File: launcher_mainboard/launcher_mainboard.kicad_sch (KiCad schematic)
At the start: 79 parts, among them J1 USB_B_Micro, J10 pin headers, J2 Conn_01x06, J3 Conn_01x06, J4 Conn_01x06, J5 Conn_01x06, J6 bat_con, J7 fan_con, J8 ESC_1, J9 ESC_2, Q1 2N7002H, Q2 2N3904, Q3 2N3904, Q4 BSS138, Q5 BSS138, Q6 BSS138, Q7 BSS138, SW1 POWER_SWITCH, U1 ESP32-S3-MINI-1, U12 LM66200DRLR, U2 TMC2209-LA-T, U3 TMC2209-LA-T, U4 TMC2209-LA-T, U5 TMC2209-LA-T, U6 TLV75801PDRV, U7 R-78E3.3-0.5, U8 D3V3XA4B10LP, U9 R-78E5.0-0.5

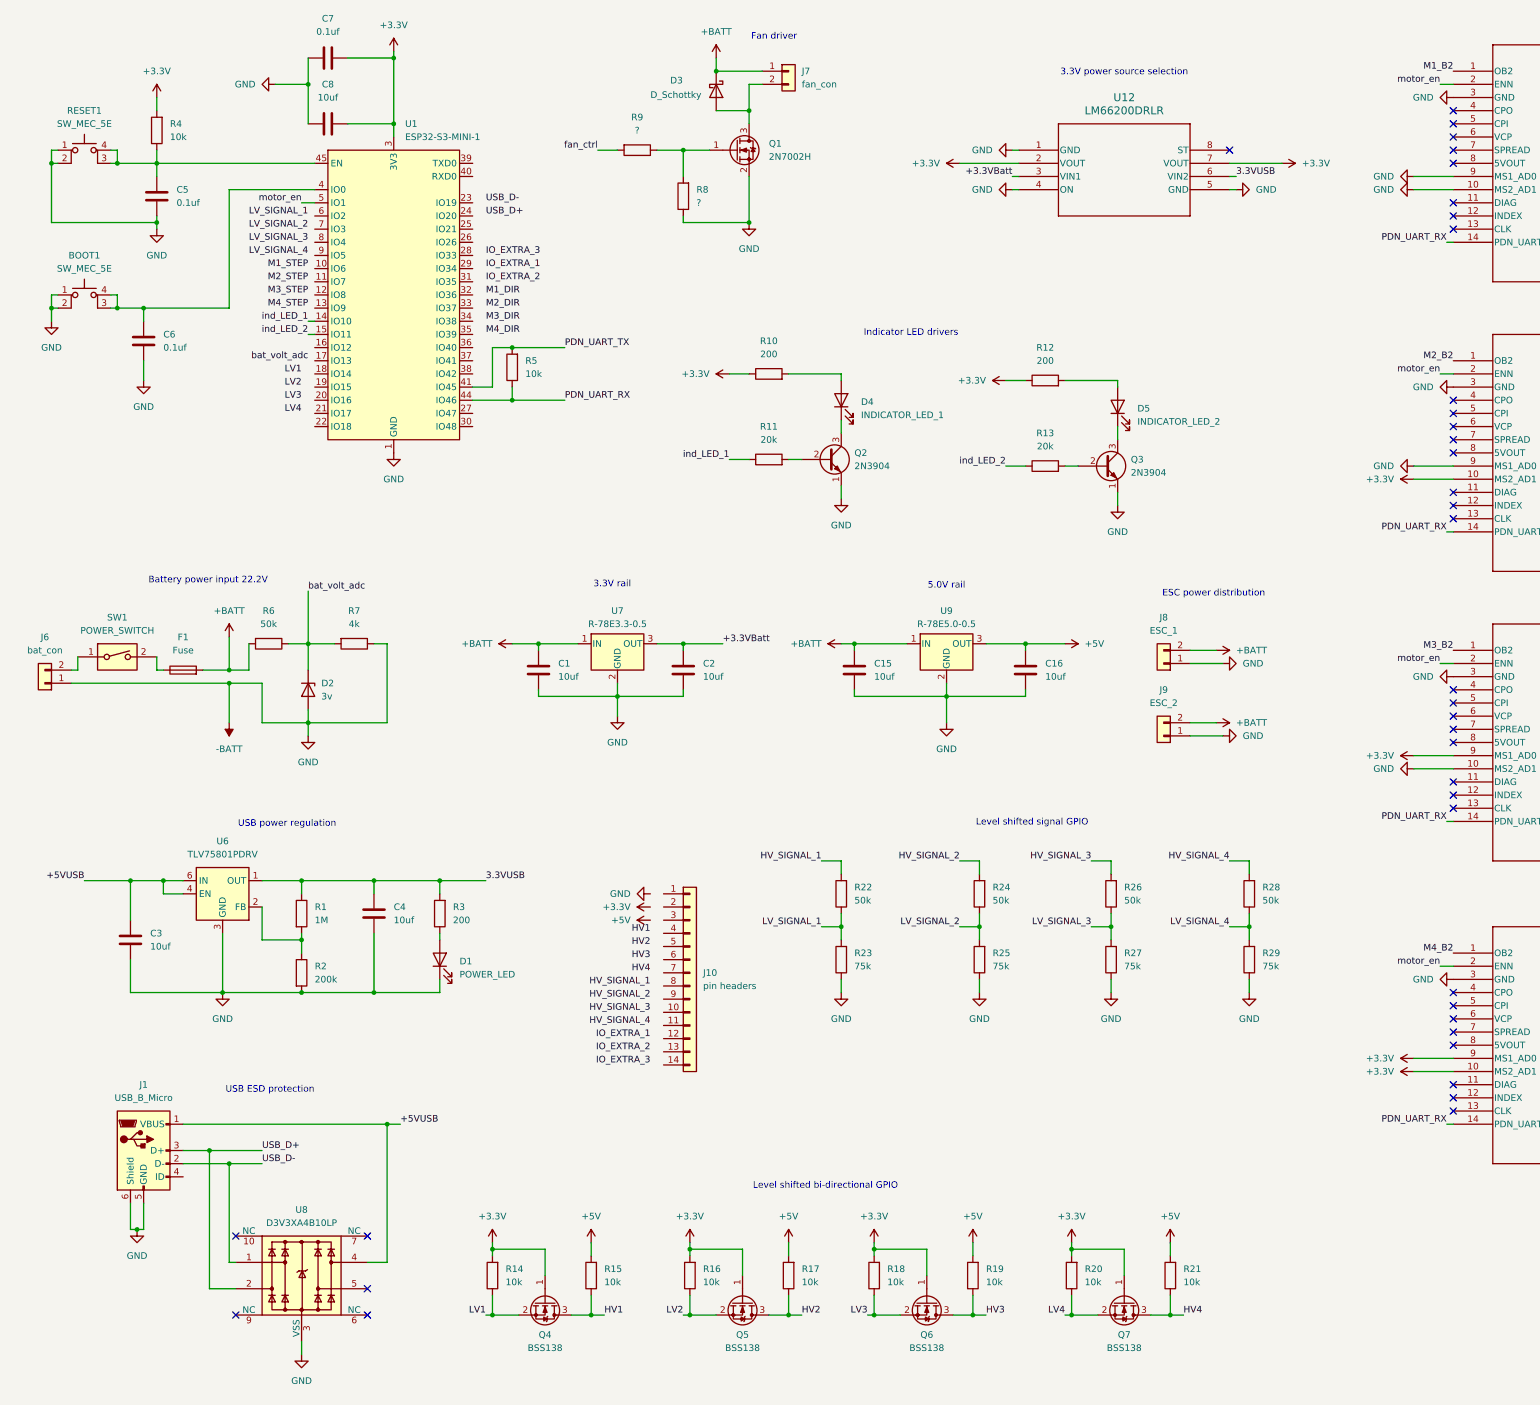
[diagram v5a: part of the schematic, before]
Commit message: first complete scematic draft
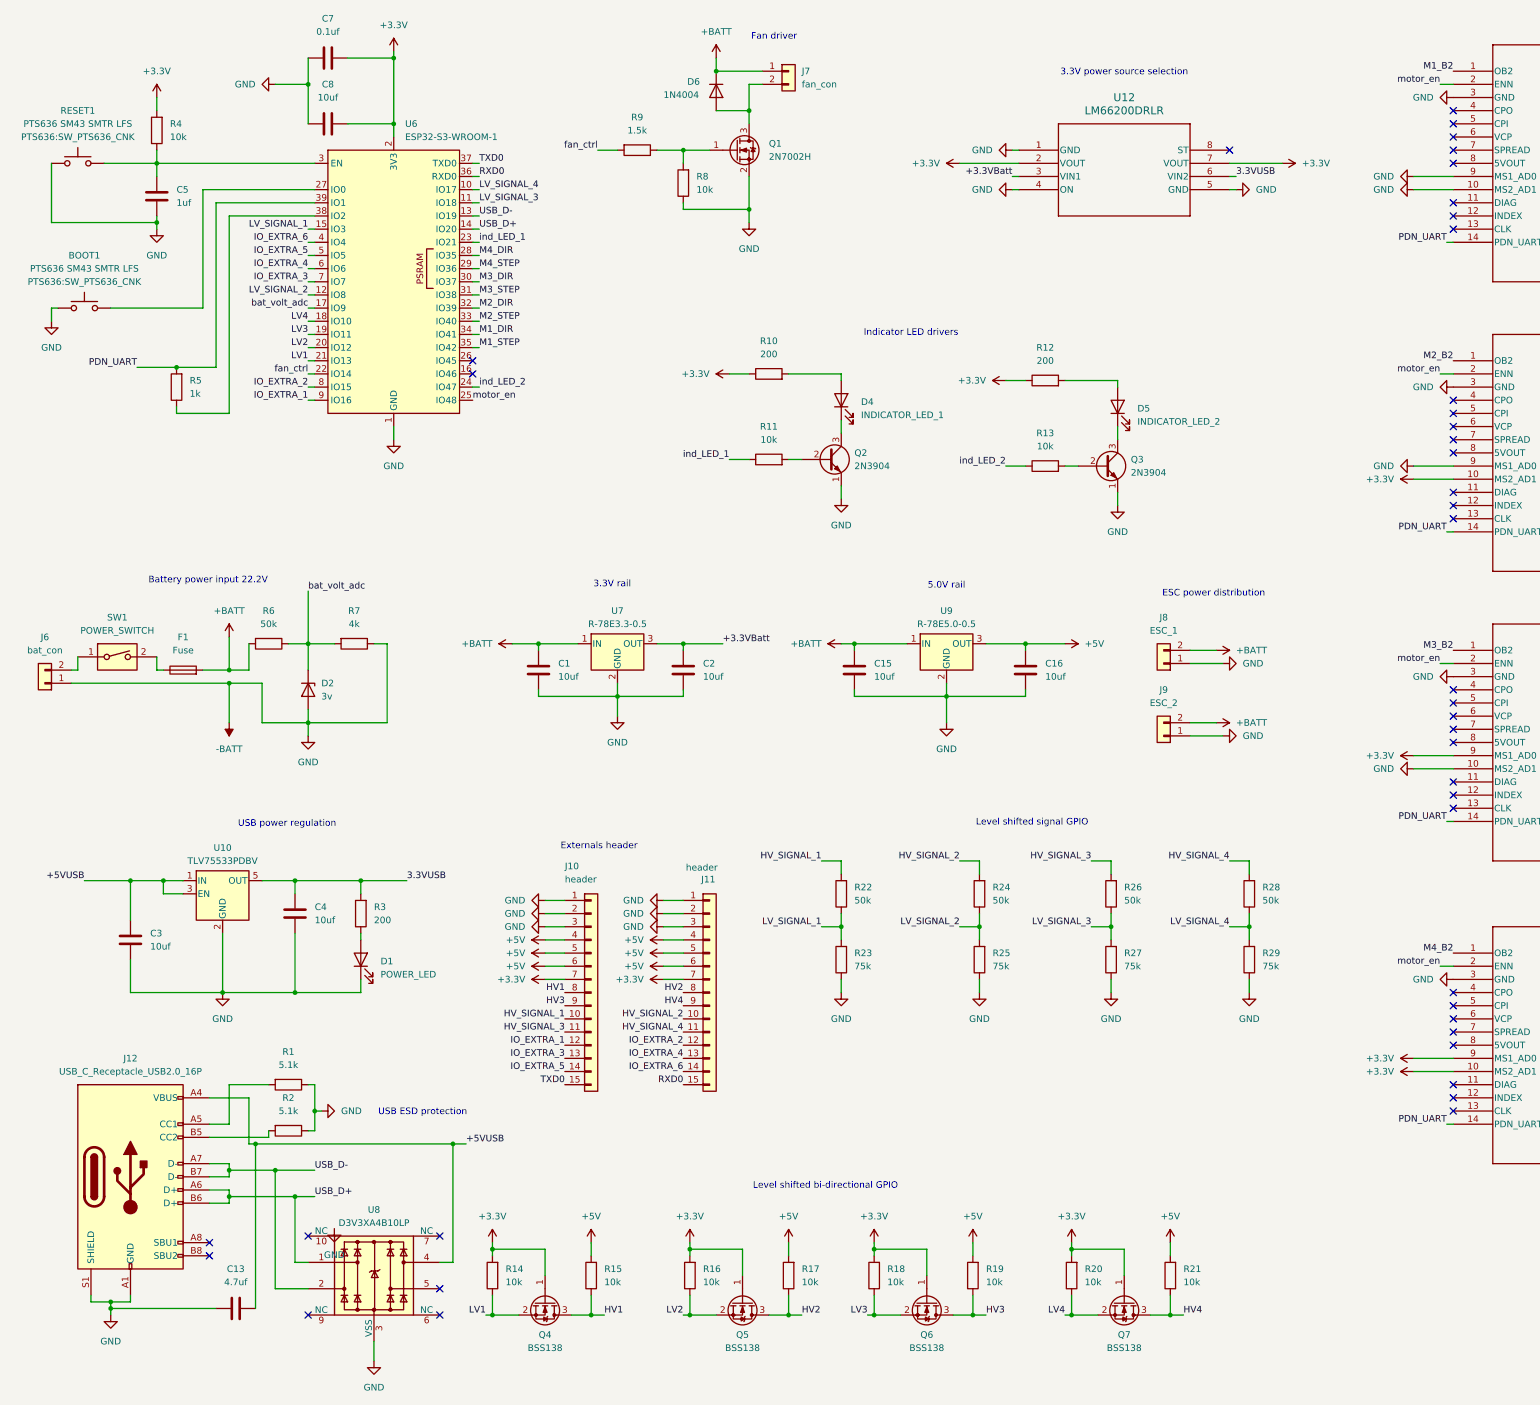
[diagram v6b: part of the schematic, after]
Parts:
- removed BOOT1, RESET1: SW_MEC_5E, Button_Switch_SMD:SW_MEC_5GSH9, symbol Switch:SW_MEC_5E
- removed C6: 0.1uf, Capacitor_SMD:C_0201_0603Metric, symbol Device:C
- removed D3: D_Schottky, Diode_SMD:D_0201_0603Metric, symbol Device:D_Schottky
- removed J1: USB_B_Micro, Connector_USB:USB_Micro-B_Amphenol_10104110_Horizontal, symbol Connector:USB_B_Micro
- removed J10: pin headers, Connector_PinHeader_2.54mm:PinHeader_1x14_P2.54mm_Vertical, symbol Connector_Generic:Conn_01x14
- removed U1: ESP32-S3-MINI-1, RF_Module:ESP32-S2-MINI-1, symbol RF_Module:ESP32-S3-MINI-1
- removed U6: TLV75801PDRV, Package_SON:WSON-6-1EP_2x2mm_P0.65mm_EP1x1.6mm, symbol Regulator_Linear:TLV75801PDRV
- added BOOT1, RESET1: PTS636 SM43 SMTR LFS, PTS636:SW_PTS636_CNK, symbol Switch:SW_Push
- added C13: 4.7uf, Capacitor_SMD:C_0805_2012Metric, symbol Device:C
- added D6: 1N4004, Diode_THT:D_DO-35_SOD27_P5.08mm_Vertical_KathodeUp, symbol Diode:1N4004
- added J10, J11: header, Connector_PinHeader_2.54mm:PinHeader_1x15_P2.54mm_Vertical, symbol Connector_Generic:Conn_01x15
- added J12: USB_C_Receptacle_USB2.0_16P, Connector_USB:USB_C_Receptacle_G-Switch_GT-USB-7010ASV, symbol Connector:USB_C_Receptacle_USB2.0_16P
- added U10: TLV75533PDBV, Package_TO_SOT_SMD:SOT-23-5, symbol Regulator_Linear:TLV75533PDBV
- added U6: ESP32-S3-WROOM-1, RF_Module:ESP32-S3-WROOM-1, symbol RF_Module:ESP32-S3-WROOM-1
- C1, C15, C16, C2, C3, C4, C7, C8: footprint Capacitor_SMD:C_0201_0603Metric -> Capacitor_SMD:C_0805_2012Metric
- C5: value 0.1uf -> 1uf; footprint Capacitor_SMD:C_0201_0603Metric -> Capacitor_SMD:C_0805_2012Metric
- R1: value 1M -> 5.1k; footprint Resistor_SMD:R_0201_0603Metric -> Resistor_SMD:R_0805_2012Metric
- R10, R12, R14, R15, R16, R17, R18, R19, R20, R21, R22, R23, R24, R25, R26, R27, R28, R29, R3, R4, R6, R7: footprint Resistor_SMD:R_0201_0603Metric -> Resistor_SMD:R_0805_2012Metric
- R11, R13: value 20k -> 10k; footprint Resistor_SMD:R_0201_0603Metric -> Resistor_SMD:R_0805_2012Metric
- R2: value 200k -> 5.1k; footprint Resistor_SMD:R_0201_0603Metric -> Resistor_SMD:R_0805_2012Metric
- R5: value 10k -> 1k; footprint Resistor_SMD:R_0201_0603Metric -> Resistor_SMD:R_0805_2012Metric
- R8: value ? -> 10k; footprint Resistor_SMD:R_0201_0603Metric -> Resistor_SMD:R_0805_2012Metric
- R9: value ? -> 1.5k; footprint Resistor_SMD:R_0201_0603Metric -> Resistor_SMD:R_0805_2012Metric
- SW1: footprint (none) -> Button_Switch_SMD:SW_DIP_SPSTx01_Slide_9.78x4.72mm_W8.61mm_P2.54mm
- U3, U4, U5: footprint TMC2209-LA-T:QFN28_5X5_3X8_EPAD_TRI -> CustomFootprints:TCM2209_Module
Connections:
- net PDN_UART_TX is gone; now on net PDN_UART: R5.2
- net +3.3V: now also J10.7 (Pin_7), J11.7 (Pin_7), U6.2 (3V3)
- net +5V: now also J10.4 (Pin_4), J10.5 (Pin_5), J10.6 (Pin_6), J11.4 (Pin_4), J11.5 (Pin_5), J11.6 (Pin_6)
- net +5VUSB: now also C13.1, J12.A4 (VBUS), J12.A9 (VBUS), J12.B4 (VBUS), J12.B9 (VBUS), U10.1 (IN), U10.3 (EN)
- net +BATT: now also D6.1 (K)
- net -BATT: now also R1.1, R2.1, BOOT1.1, C13.2, J10.1 (Pin_1), J10.2 (Pin_2), J10.3 (Pin_3), J11.1 (Pin_1), J11.2 (Pin_2), J11.3 (Pin_3), J12.A1 (GND), J12.A12 (GND), J12.B1 (GND), J12.B12 (GND), J12.S1 (SHIELD), RESET1.1, U10.2 (GND), U6.1 (GND), U6.40 (GND), U6.41 (GND); no longer R2.2
- net 3.3VUSB: now also U10.5 (OUT); no longer R1.1
- net HV1: now also J10.8 (Pin_8)
- net HV2: now also J11.8 (Pin_8)
- net HV3: now also J10.9 (Pin_9)
- net HV4: now also J11.9 (Pin_9)
- net HV_SIGNAL_1: now also J10.10 (Pin_10)
- net HV_SIGNAL_2: now also J11.10 (Pin_10)
- net HV_SIGNAL_3: now also J10.11 (Pin_11)
- net HV_SIGNAL_4: now also J11.11 (Pin_11)
- net IO_EXTRA_1: now also J10.12 (Pin_12), U6.9 (IO16)
- net IO_EXTRA_2: now also J11.12 (Pin_12), U6.8 (IO15)
- net IO_EXTRA_3: now also J10.13 (Pin_13), U6.7 (IO7)
- net LV1: now also U6.21 (IO13)
- net LV2: now also U6.20 (IO12)
- net LV3: now also U6.19 (IO11)
- net LV4: now also U6.18 (IO10)
- net LV_SIGNAL_1: now also U6.15 (IO3)
- net LV_SIGNAL_2: now also U6.12 (IO8)
- net LV_SIGNAL_3: now also U6.11 (IO18)
- net LV_SIGNAL_4: now also U6.10 (IO17)
- net M1_DIR: now also U6.34 (IO41)
- net M1_STEP: now also U6.35 (IO42)
- net M2_DIR: now also U6.32 (IO39)
- net M2_STEP: now also U6.33 (IO40)
- net M3_DIR: now also U6.30 (IO37)
- net M3_STEP: now also U6.31 (IO38)
- net M4_DIR: now also U6.28 (IO35)
- net M4_STEP: now also U6.29 (IO36)
- net USB_D+: now also U8.1, J12.A6 (D+), J12.B6 (D+), U6.14 (IO20); no longer U8.2
- net USB_D-: now also U8.2, J12.A7 (D-), J12.B7 (D-), U6.13 (IO19); no longer U8.1
- net bat_volt_adc: now also U6.17 (IO9)
- net fan_ctrl: now also U6.22 (IO14)
- net ind_LED_1: now also U6.23 (IO21)
- net ind_LED_2: now also U6.24 (IO47)
- net motor_en: now also U6.25 (IO48)
- net at R1.2: now also J12.A5 (CC1); no longer R2.1
- net at J7.2 (Pin_2), Q1.3 (D): now also D6.2 (A)
- net at C5.1, R4.1: now also RESET1.2, U6.3 (EN)
- net PDN_UART_RX renamed PDN_UART
- net PDN_UART: now also U6.39 (IO1); no longer R5.1
- new net: J12.B5 (CC2), R2.2
- new net: BOOT1.2, U6.27 (IO0)
- new net: R5.1, U6.38 (IO2)
- new net IO_EXTRA_4: J11.13 (Pin_13), U6.6 (IO6)
- new net IO_EXTRA_5: J10.14 (Pin_14), U6.5 (IO5)
- new net IO_EXTRA_6: J11.14 (Pin_14), U6.4 (IO4)
- new net RXD0: J11.15 (Pin_15), U6.36 (RXD0)
- new net TXD0: J10.15 (Pin_15), U6.37 (TXD0)
- no-connect marks 54 -> 58
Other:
- note added: "Externals header"
- moved on the sheet: C4, D1, R3, R5, R8, U8

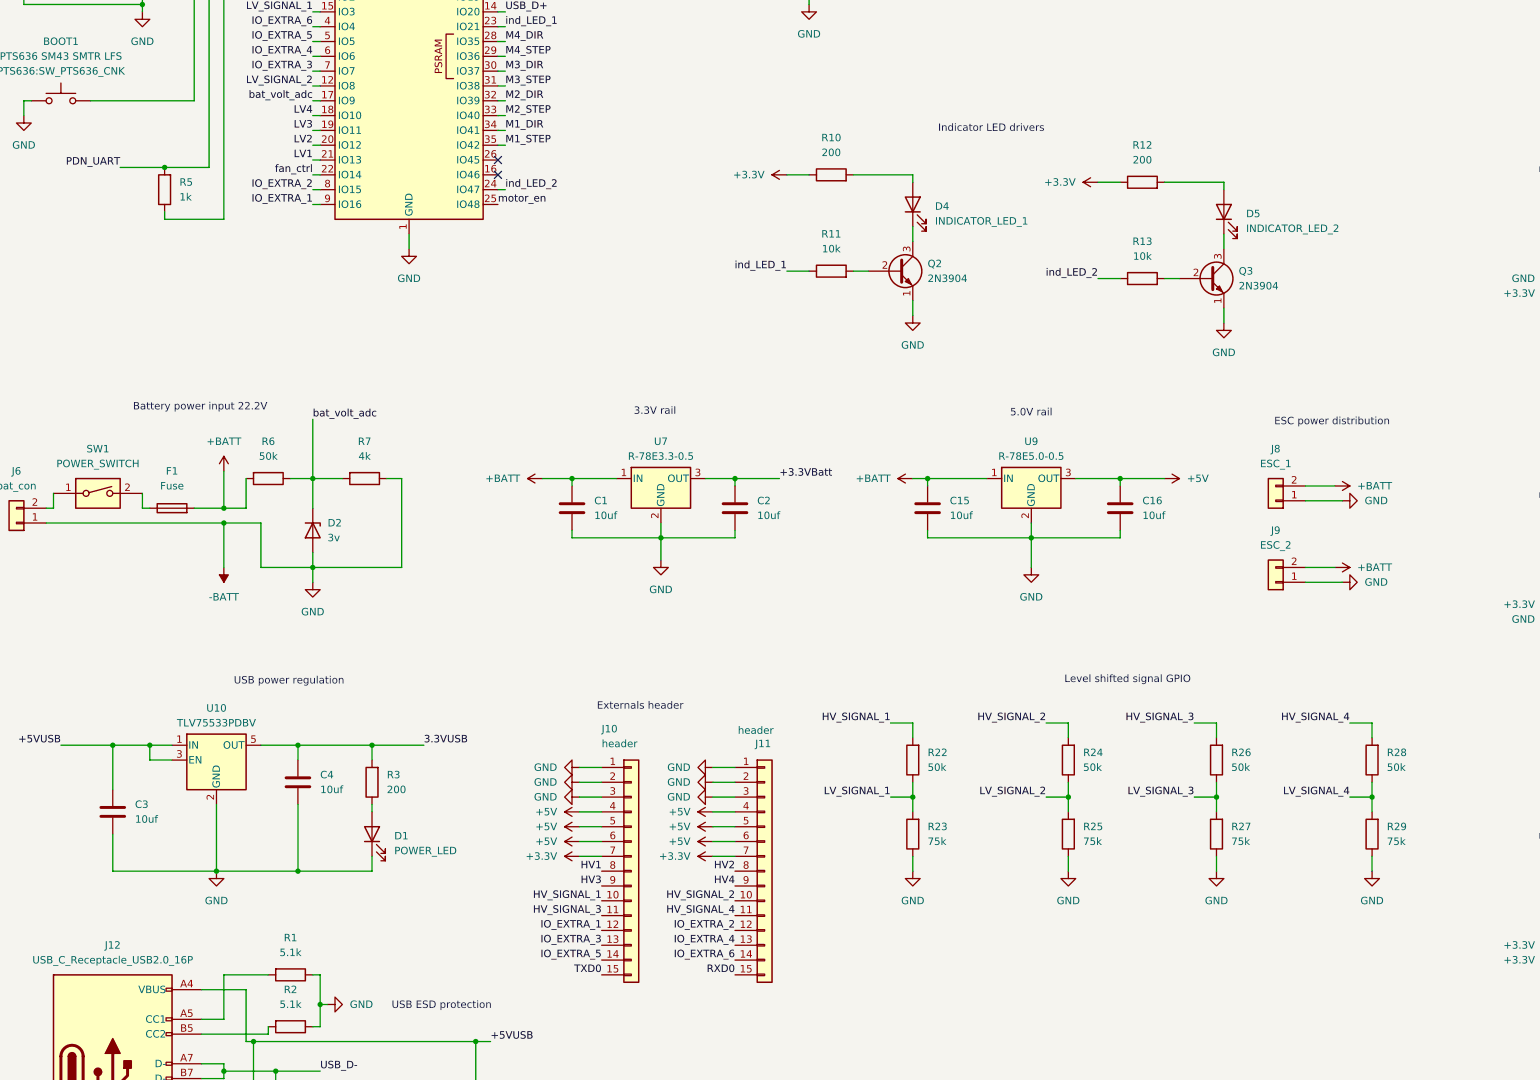
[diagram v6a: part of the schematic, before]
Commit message: added more footprints. Rought layout
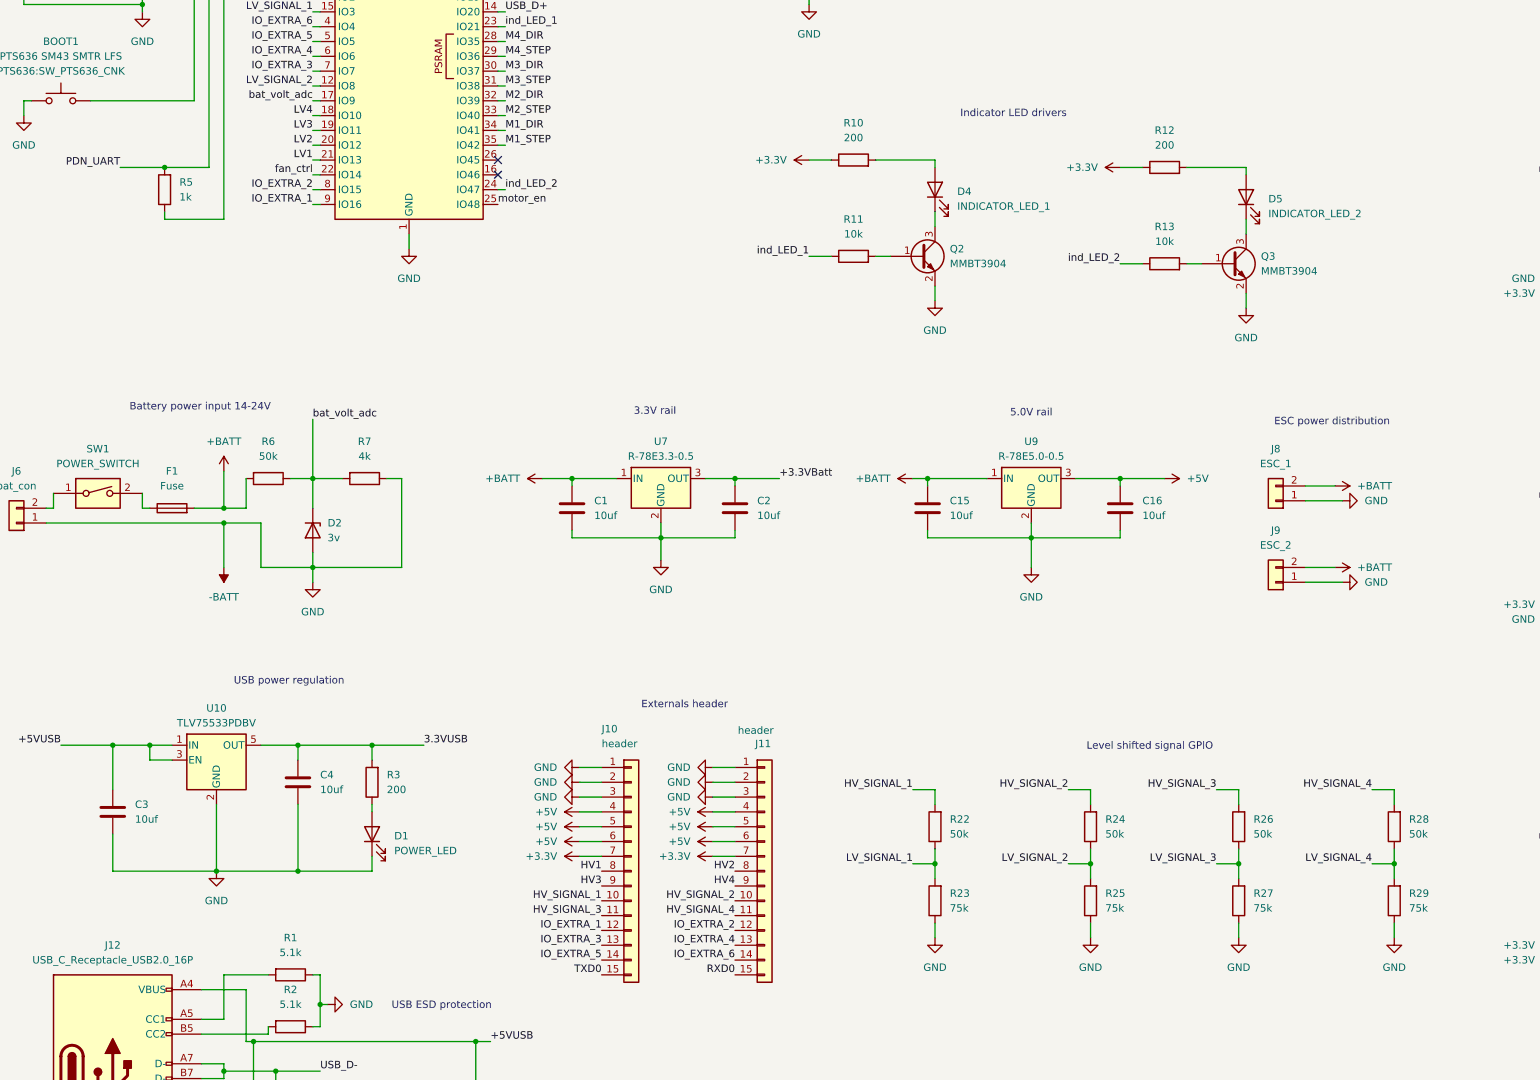
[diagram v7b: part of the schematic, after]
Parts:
- removed Q2, Q3: 2N3904, Package_TO_SOT_THT:TO-92_Inline, symbol Transistor_BJT:2N3904
- added Q2, Q3: MMBT3904, Package_TO_SOT_SMD:SOT-23, symbol Transistor_BJT:MMBT3904
- F1: footprint Fuse:FuseHolder_Blade_ATO_Littelfuse_FLR_178.6165 -> Fuse:Fuseholder_Clip-5x20mm_Bel_FC-203-22_Lateral_P17.80x5.00mm_D1.17mm_Horizontal
- J12: footprint Connector_USB:USB_C_Receptacle_G-Switch_GT-USB-7010ASV -> Connector_USB:USB_C_Receptacle_JAE_DX07S016JA1R1500
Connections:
- net -BATT: now also Q2.2 (E), Q3.2 (E)
- net at D4.1 (K): now also Q2.3 (C)
- net at R13.2: now also Q3.1 (B)
- net at D5.1 (K): now also Q3.3 (C)
- net at R11.2: now also Q2.1 (B)
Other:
- note added: "Battery power input 14-24V"
- note removed: "Battery power input 22.2V"
- moved on the sheet: D4, D5, R10, R11, R12, R13, R22, R23, R24, R25, R26, R27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

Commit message: more layout
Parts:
- C10, C11, C12, C9: footprint Capacitor_SMD:CP_Elec_3x5.3 -> Capacitor_SMD:CP_Elec_8x10.5
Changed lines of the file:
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@@
 			)
 		)
-		(property "Footprint" "Capacitor_SMD:CP_Elec_3x5.3"
+		(property "Footprint" "Capacitor_SMD:CP_Elec_8x10.5"
 			(at 361.95 208.28 0)
 			(effects
@@
 			)
 		)
-		(property "Footprint" "Capacitor_SMD:CP_Elec_3x5.3"
+		(property "Footprint" "Capacitor_SMD:CP_Elec_8x10.5"
 			(at 361.95 149.86 0)
 			(effects
@@
 			)
 		)
-		(property "Footprint" "Capacitor_SMD:CP_Elec_3x5.3"
+		(property "Footprint" "Capacitor_SMD:CP_Elec_8x10.5"
 			(at 361.95 93.98 0)
 			(effects
@@
 			)
 		)
-		(property "Footprint" "Capacitor_SMD:CP_Elec_3x5.3"
+		(property "Footprint" "Capacitor_SMD:CP_Elec_8x10.5"
 			(at 361.95 38.1 0)
 			(effects
